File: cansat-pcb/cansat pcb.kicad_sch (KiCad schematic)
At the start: 19 parts, among them J1 Conn_01x03_Pin, J2 Conn_01x03_Pin, J3 Conn_01x03_Pin, Q1 2N3904, Q2 AO3400A, SW1 SW_DPDT_x2, U3 MPU6050

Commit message: LAATSTE VERSIE!!!!!!
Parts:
- removed J1, J2, J3: Conn_01x03_Pin, Connector_PinHeader_1.00mm:PinHeader_1x03_P1.00mm_Vertical, symbol Connector:Conn_01x03_Pin
- removed M1: ~, CanSat:PowerBoost, symbol CanSat:adafruit_PowerBoost_1000c
- removed Q1: 2N3904, Package_TO_SOT_THT:TO-92_Inline, symbol Transistor_BJT:2N3904
- removed Q2: AO3400A, Package_TO_SOT_SMD:SOT-23, symbol Transistor_FET:AO3400A
- removed R1, R5: 1K, Resistor_SMD:R_0805_2012Metric_Pad1.20x1.40mm_HandSolder, symbol Device:R
- removed R2: 22K, Resistor_SMD:R_0805_2012Metric_Pad1.20x1.40mm_HandSolder, symbol Device:R
- removed R3, R4: 100K, Resistor_SMD:R_0805_2012Metric_Pad1.20x1.40mm_HandSolder, symbol Device:R
- removed S1: ~, CanSat:BMP280, symbol CanSat:BMP280
- removed U1: ~, CanSat:RFM69HCW, symbol CanSat:RFM69HCW
- removed U2: ~, CanSat:KPEG132, symbol CanSat:KPEG132
- removed U3: MPU6050, CanSat:MPU6050, symbol CanSat:MPU6050
- removed U4, U5: ~, Package_TO_SOT_THT:TO-92L_Inline, symbol CanSat:TMP36
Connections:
- net TMP1: now reaches MCU1.31 (GP26)
- net BUZZER: no longer names the net of MCU1.32 (GP27)
- net SERVO_1 renamed SERVO/SERVO 1
- net SERVO_2 renamed SERVO/SERVO 2
- net SERVO_3 renamed SERVO/SERVO 3
- net TMP36_1: no longer names the net of MCU1.27 (GP21)
- net TMP36_2 renamed buzzer
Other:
- added sheet BATTERY (BATTERY.kicad_sch)
- added sheet BME688 (BMP280.kicad_sch)
- added sheet BUZZER (buzzer.kicad_sch)
- added sheet CO2 & VOCs (untitled.kicad_sch)
- added sheet GYRO (GYRO.kicad_sch)
- added sheet RADIO (RADIO.kicad_sch)
- added sheet SERVO (servo.kicad_sch)
- added sheet SGP30 (SGP30.kicad_sch)
- added sheet TEMPERATURE (TEMPERATURE.kicad_sch)
- moved on the sheet: SW1A

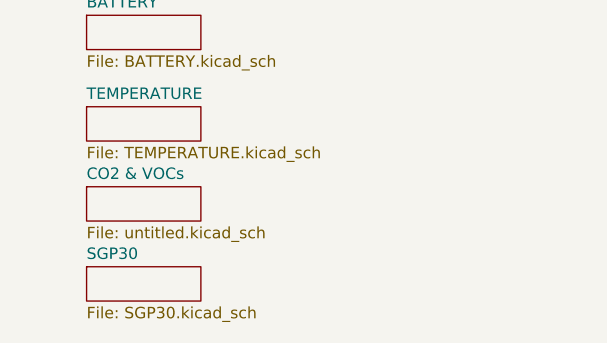
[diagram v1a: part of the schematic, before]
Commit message: delete unused file
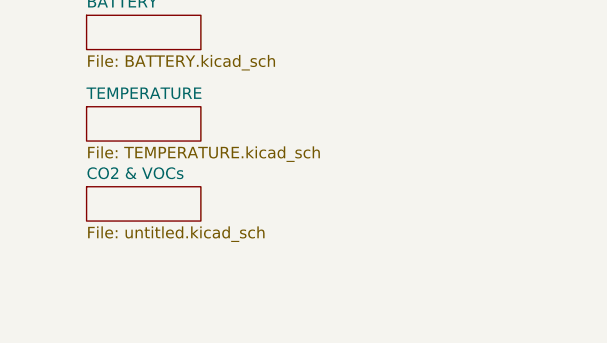
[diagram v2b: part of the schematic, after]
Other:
- removed sheet SGP30
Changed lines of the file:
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@@
-    )
-  )
-  (sheet (at 49.53 128.27) (size 12.7 3.81) (fields_autoplaced)
-    (stroke (width 0.1524) (type solid))
-    (fill (color 0 0 0 0.0000))
-    (property "Sheetname" "SGP30" (at 49.53 127.5584 0)
-      (effects (font (size 1.27 1.27)) (justify left bottom))
-    )
-    (property "Sheetfile" "SGP30.kicad_sch" (at 49.53 132.6646 0)
-      (effects (font (size 1.27 1.27)) (justify left top))
-    )
-    (instances
-      (project "cansat pcb"
-        (path "/5b536bad-dff4-4fc1-b4ee-d4495f6592c9" (page "10"))
-      )
     )
   )
